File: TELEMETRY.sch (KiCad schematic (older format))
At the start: 0 parts

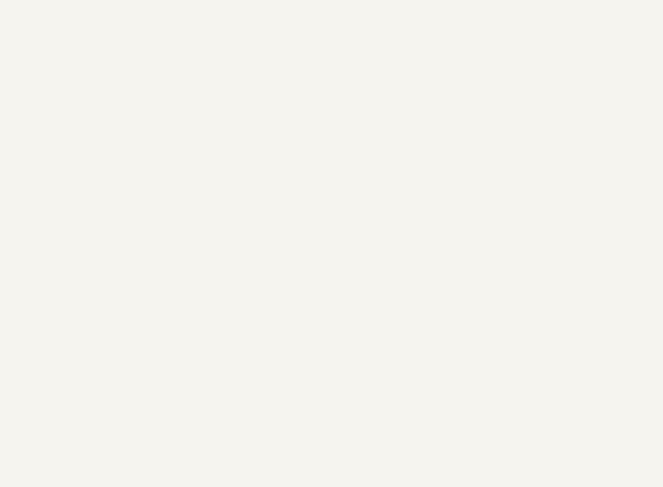
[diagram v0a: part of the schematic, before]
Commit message: Added RFM95
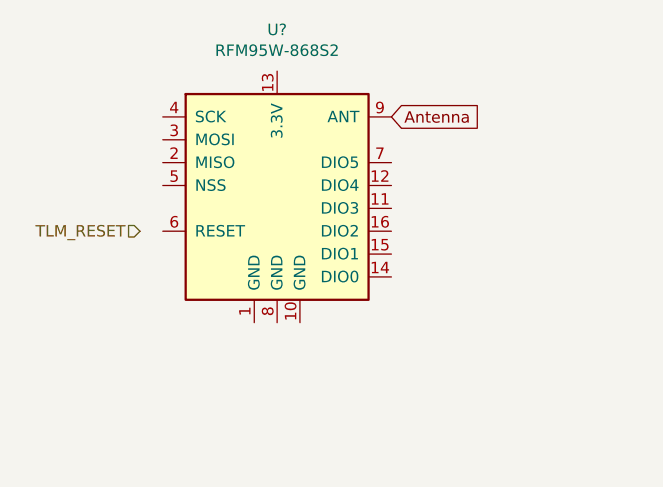
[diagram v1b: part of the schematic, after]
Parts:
- added U?: RFM95W-868S2, symbol RF_Module:RFM95W-868S2
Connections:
- new net Antenna: U?.9 (ANT)
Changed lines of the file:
@@
 $Descr A4 11693 8268
 encoding utf-8
-Sheet 4 9
+Sheet 9 9
 Title "TARS-MK1"
 Date ""
@@
 	1    0    0    -1
 $EndComp
+$Comp
+L RF_Module:RFM95W-868S2 U?
+U 1 1 5F8B4512
+P 3500 2950
+F 0 "U?" H 3500 3631 50  0000 C CNN
+F 1 "RFM95W-868S2" H 3500 3540 50  0000 C CNN
+F 2 "" H 200 4600 50  0001 C CNN
+F 3 "https://www.hoperf.com/data/upload/portal/20181127/5bfcbea20e9ef.pdf" H 200 4600 50  0001 C CNN
+	1    3500 2950
+	1    0    0    -1
+$EndComp
+Text GLabel 4000 2650 2    50   Input ~ 0
+Antenna
+Text HLabel 2900 3150 0    50   Input ~ 0
+TLM_RESET
 $EndSCHEMATC

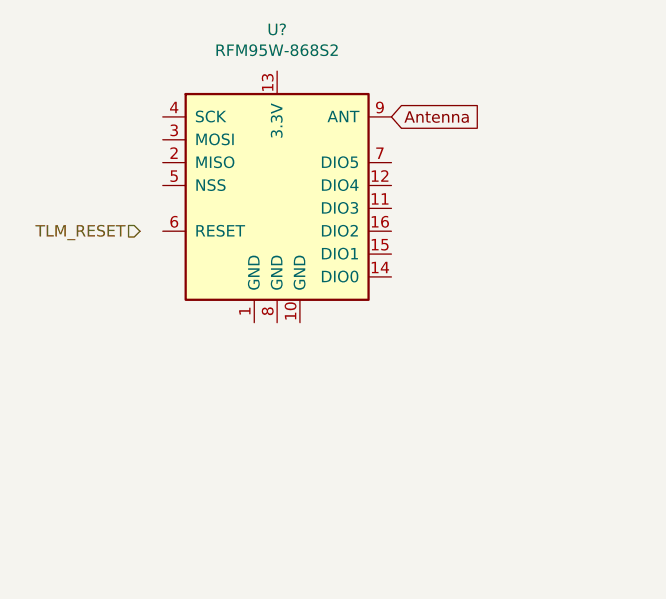
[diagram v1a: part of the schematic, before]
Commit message: Added labels to RFM95
Hierarchical and global labels added, as well as sheet labels
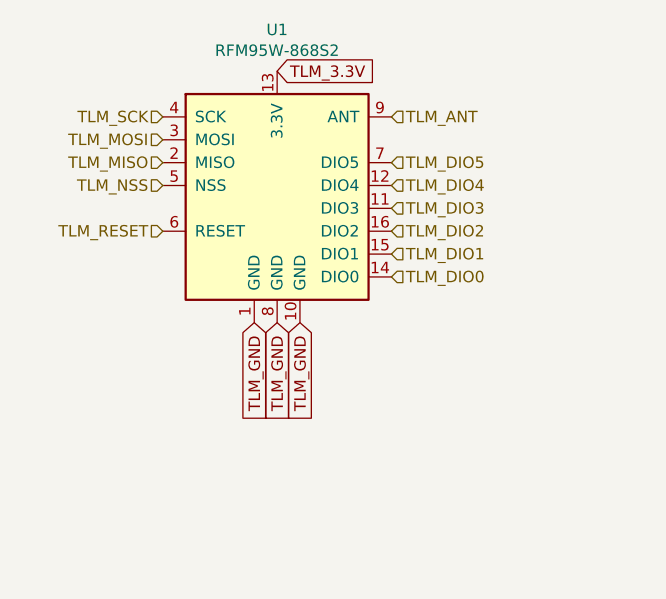
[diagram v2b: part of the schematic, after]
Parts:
- gave numbers to parts that had none: 1
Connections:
- net TLM_RESET: now also U1.6 (RESET)
- net TLM_GND: now reaches U1.1 (GND)
- net TLM_GND: now also U1.10 (GND), U1.8 (GND)
- net TLM_DIO3: now reaches U1.11 (DIO3)
- net TLM_DIO4: now reaches U1.12 (DIO4)
- net TLM_3.3V: now reaches U1.13 (3.3V)
- net TLM_DIO0: now reaches U1.14 (DIO0)
- net TLM_DIO1: now reaches U1.15 (DIO1)
- net TLM_DIO2: now reaches U1.16 (DIO2)
- net TLM_MISO: now reaches U1.2 (MISO)
- net TLM_MOSI: now reaches U1.3 (MOSI)
- net TLM_SCK: now reaches U1.4 (SCK)
- net TLM_NSS: now reaches U1.5 (NSS)
- net TLM_DIO5: now reaches U1.7 (DIO5)
- net Antenna renamed TLM_ANT
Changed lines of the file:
@@
 $EndDescr
 $Comp
-L ISS_LOGO:LOGO #G?
+L ISS_LOGO:LOGO #G9
 U 1 1 5F87BCA1
 P 7600 6800
-F 0 "#G?" H 7600 6677 60  0001 C CNN
+F 0 "#G9" H 7600 6677 60  0001 C CNN
 F 1 "LOGO" H 7600 6923 60  0001 C CNN
 F 2 "" H 7600 6800 50  0001 C CNN
@@
 	1    0    0    -1
 $EndComp
+Text HLabel 3000 3150 0    50   Input ~ 0
+TLM_RESET
+Text HLabel 4000 2650 2    50   Input ~ 0
+TLM_ANT
+Text HLabel 3000 2650 0    50   Input ~ 0
+TLM_SCK
+Text HLabel 3000 2750 0    50   Input ~ 0
+TLM_MOSI
+Text HLabel 3000 2850 0    50   Input ~ 0
+TLM_MISO
+Text HLabel 3000 2950 0    50   Input ~ 0
+TLM_NSS
+Text GLabel 3400 3550 3    50   Input ~ 0
+TLM_GND
+Text GLabel 3500 3550 3    50   Input ~ 0
+TLM_GND
+Text GLabel 3600 3550 3    50   Input ~ 0
+TLM_GND
+Text HLabel 4000 2850 2    50   Input ~ 0
+TLM_DIO5
+Text HLabel 4000 2950 2    50   Input ~ 0
+TLM_DIO4
+Text HLabel 4000 3050 2    50   Input ~ 0
+TLM_DIO3
+Text HLabel 4000 3150 2    50   Input ~ 0
+TLM_DIO2
+Text HLabel 4000 3250 2    50   Input ~ 0
+TLM_DIO1
+Text HLabel 4000 3350 2    50   Input ~ 0
+TLM_DIO0
 $Comp
-L RF_Module:RFM95W-868S2 U?
+L RF_Module:RFM95W-868S2 U1
 U 1 1 5F8B4512
 P 3500 2950
-F 0 "U?" H 3500 3631 50  0000 C CNN
+F 0 "U1" H 3500 3631 50  0000 C CNN
 F 1 "RFM95W-868S2" H 3500 3540 50  0000 C CNN
 F 2 "" H 200 4600 50  0001 C CNN
@@
 	1    0    0    -1
 $EndComp
-Text GLabel 4000 2650 2    50   Input ~ 0
-Antenna
-Text HLabel 2900 3150 0    50   Input ~ 0
-TLM_RESET
+Text GLabel 3500 2450 2    50   Input ~ 0
+TLM_3.3V
 $EndSCHEMATC

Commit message: Added SMA connector
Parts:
- added X1: SMACONNECTOR, symbol SMA_CONNECTOR:SMACONNECTOR
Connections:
- net labels added: 3.3V_IN, GND
- net labels removed: TLM_3.3V, TLM_ANT, TLM_GND
- wire segments 0 -> 10
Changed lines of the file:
@@
 Text HLabel 3000 3150 0    50   Input ~ 0
 TLM_RESET
-Text HLabel 4000 2650 2    50   Input ~ 0
-TLM_ANT
 Text HLabel 3000 2650 0    50   Input ~ 0
 TLM_SCK
@@
 Text HLabel 3000 2950 0    50   Input ~ 0
 TLM_NSS
-Text GLabel 3400 3550 3    50   Input ~ 0
-TLM_GND
-Text GLabel 3500 3550 3    50   Input ~ 0
-TLM_GND
-Text GLabel 3600 3550 3    50   Input ~ 0
-TLM_GND
 Text HLabel 4000 2850 2    50   Input ~ 0
 TLM_DIO5
@@
 $EndComp
 Text GLabel 3500 2450 2    50   Input ~ 0
-TLM_3.3V
+3.3V_IN
+$Comp
+L power:GND #PWR01
+U 1 1 5F947841
+P 3500 3700
+F 0 "#PWR01" H 3500 3450 50  0001 C CNN
+F 1 "GND" H 3505 3527 50  0000 C CNN
+F 2 "" H 3500 3700 50  0001 C CNN
+F 3 "" H 3500 3700 50  0001 C CNN
+	1    3500 3700
+	1    0    0    -1
+$EndComp
+Wire Wire Line
+	3400 3550 3500 3550
+Connection ~ 3500 3550
+Wire Wire Line
+	3500 3550 3600 3550
+Wire Wire Line
+	3500 3550 3500 3700
+$Comp
+L SMA_CONNECTOR:SMACONNECTOR X1
+U 1 1 5F9480D1
+P 4800 2650
+F 0 "X1" H 5030 2696 50  0000 L CNN
+F 1 "SMACONNECTOR" H 5030 2605 50  0000 L CNN
+F 2 "" H 4800 2650 50  0001 C CNN
+F 3 "" H 4800 2650 50  0001 C CNN
+	1    4800 2650
+	1    0    0    -1
+$EndComp
+Wire Wire Line
+	4000 2650 4500 2650
+$Comp
+L power:GND #PWR03
+U 1 1 5F949889
+P 4800 3050
+F 0 "#PWR03" H 4800 2800 50  0001 C CNN
+F 1 "GND" H 4805 2877 50  0000 C CNN
+F 2 "" H 4800 3050 50  0001 C CNN
+F 3 "" H 4800 3050 50  0001 C CNN
+	1    4800 3050
+	1    0    0    -1
+$EndComp
+Wire Wire Line
+	4700 2950 4800 2950
+Wire Wire Line
+	4800 2950 4800 3050
+Connection ~ 4800 2950
+Wire Wire Line
+	4800 2950 4900 2950
+$Comp
+L power:GND #PWR02
+U 1 1 5F949FA5
+P 4800 2250
+F 0 "#PWR02" H 4800 2000 50  0001 C CNN
+F 1 "GND" H 4805 2077 50  0000 C CNN
+F 2 "" H 4800 2250 50  0001 C CNN
+F 3 "" H 4800 2250 50  0001 C CNN
+	1    4800 2250
+	-1   0    0    1
+$EndComp
+Wire Wire Line
+	4700 2350 4800 2350
+Wire Wire Line
+	4800 2350 4800 2250
+Connection ~ 4800 2350
+Wire Wire Line
+	4800 2350 4900 2350
 $EndSCHEMATC

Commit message: Fixes library paths
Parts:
- removed X1: SMACONNECTOR, symbol SMA_CONNECTOR:SMACONNECTOR
- added X?: SMACONNECTOR, symbol SMA:SMACONNECTOR
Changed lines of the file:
@@
 $Descr A4 11693 8268
 encoding utf-8
-Sheet 9 9
+Sheet 10 10
 Title "TARS-MK1"
 Date ""
@@
 Wire Wire Line
 	3500 3550 3500 3700
-$Comp
-L SMA_CONNECTOR:SMACONNECTOR X1
-U 1 1 5F9480D1
-P 4800 2650
-F 0 "X1" H 5030 2696 50  0000 L CNN
-F 1 "SMACONNECTOR" H 5030 2605 50  0000 L CNN
-F 2 "" H 4800 2650 50  0001 C CNN
-F 3 "" H 4800 2650 50  0001 C CNN
-	1    4800 2650
-	1    0    0    -1
-$EndComp
 Wire Wire Line
 	4000 2650 4500 2650
@@
 Wire Wire Line
 	4800 2350 4900 2350
+$Comp
+L SMA:SMACONNECTOR X?
+U 1 1 5F94DDFD
+P 4800 2650
+F 0 "X?" H 5030 2696 50  0000 L CNN
+F 1 "SMACONNECTOR" H 5030 2605 50  0000 L CNN
+F 2 "" H 4800 2650 50  0001 C CNN
+F 3 "" H 4800 2650 50  0001 C CNN
+	1    4800 2650
+	1    0    0    -1
+$EndComp
 $EndSCHEMATC

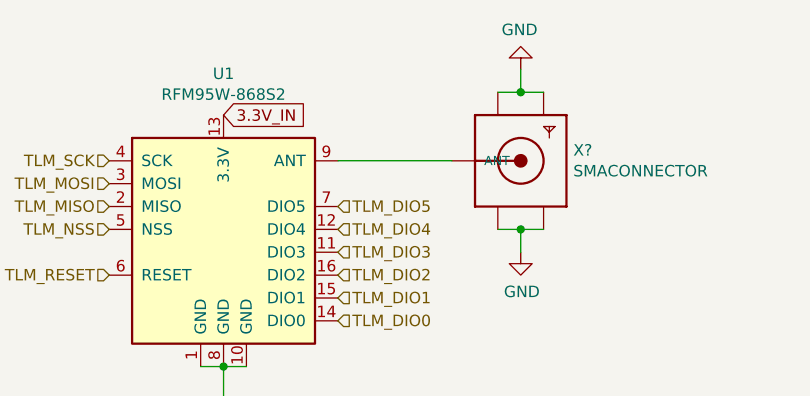
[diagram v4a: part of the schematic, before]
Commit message: Made library for D25V50F5 5V step-down
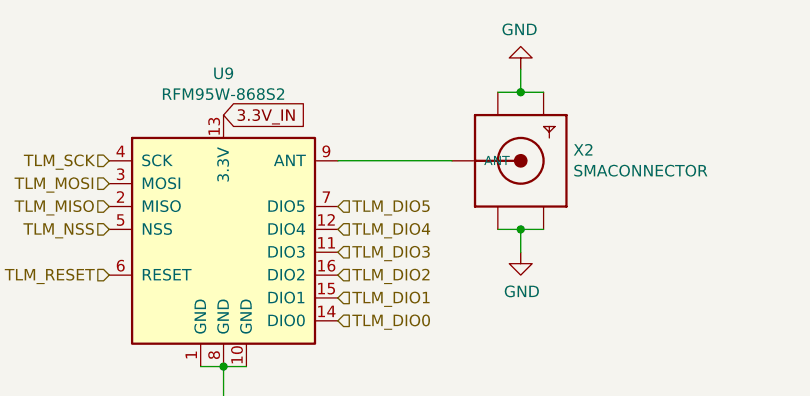
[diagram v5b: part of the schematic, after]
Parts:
- gave numbers to parts that had none: 1
- renumbered U1 to U9
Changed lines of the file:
@@
 TLM_DIO0
 $Comp
-L RF_Module:RFM95W-868S2 U1
+L RF_Module:RFM95W-868S2 U9
 U 1 1 5F8B4512
 P 3500 2950
-F 0 "U1" H 3500 3631 50  0000 C CNN
+F 0 "U9" H 3500 3631 50  0000 C CNN
 F 1 "RFM95W-868S2" H 3500 3540 50  0000 C CNN
 F 2 "" H 200 4600 50  0001 C CNN
@@
 3.3V_IN
 $Comp
-L power:GND #PWR01
+L power:GND #PWR020
 U 1 1 5F947841
 P 3500 3700
-F 0 "#PWR01" H 3500 3450 50  0001 C CNN
+F 0 "#PWR020" H 3500 3450 50  0001 C CNN
 F 1 "GND" H 3505 3527 50  0000 C CNN
 F 2 "" H 3500 3700 50  0001 C CNN
@@
 	4000 2650 4500 2650
 $Comp
-L power:GND #PWR03
+L power:GND #PWR022
 U 1 1 5F949889
 P 4800 3050
-F 0 "#PWR03" H 4800 2800 50  0001 C CNN
+F 0 "#PWR022" H 4800 2800 50  0001 C CNN
 F 1 "GND" H 4805 2877 50  0000 C CNN
 F 2 "" H 4800 3050 50  0001 C CNN
@@
 	4800 2950 4900 2950
 $Comp
-L power:GND #PWR02
+L power:GND #PWR021
 U 1 1 5F949FA5
 P 4800 2250
-F 0 "#PWR02" H 4800 2000 50  0001 C CNN
+F 0 "#PWR021" H 4800 2000 50  0001 C CNN
 F 1 "GND" H 4805 2077 50  0000 C CNN
 F 2 "" H 4800 2250 50  0001 C CNN
@@
 	4800 2350 4900 2350
 $Comp
-L SMA:SMACONNECTOR X?
+L SMA:SMACONNECTOR X2
 U 1 1 5F94DDFD
 P 4800 2650
-F 0 "X?" H 5030 2696 50  0000 L CNN
+F 0 "X2" H 5030 2696 50  0000 L CNN
 F 1 "SMACONNECTOR" H 5030 2605 50  0000 L CNN
 F 2 "" H 4800 2650 50  0001 C CNN

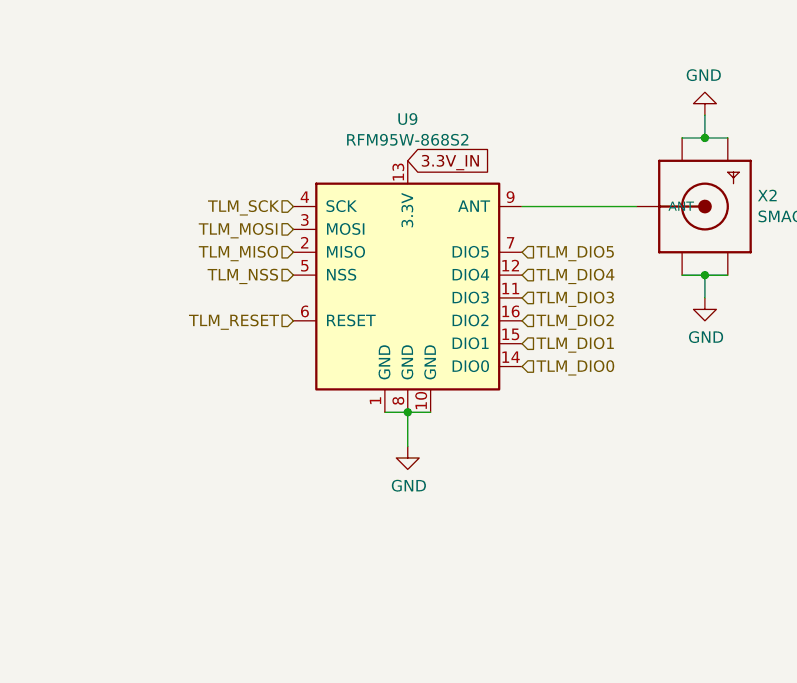
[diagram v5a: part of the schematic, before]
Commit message: Connected MPU, reorganized power system, cleaned libraries, created BBB footprint
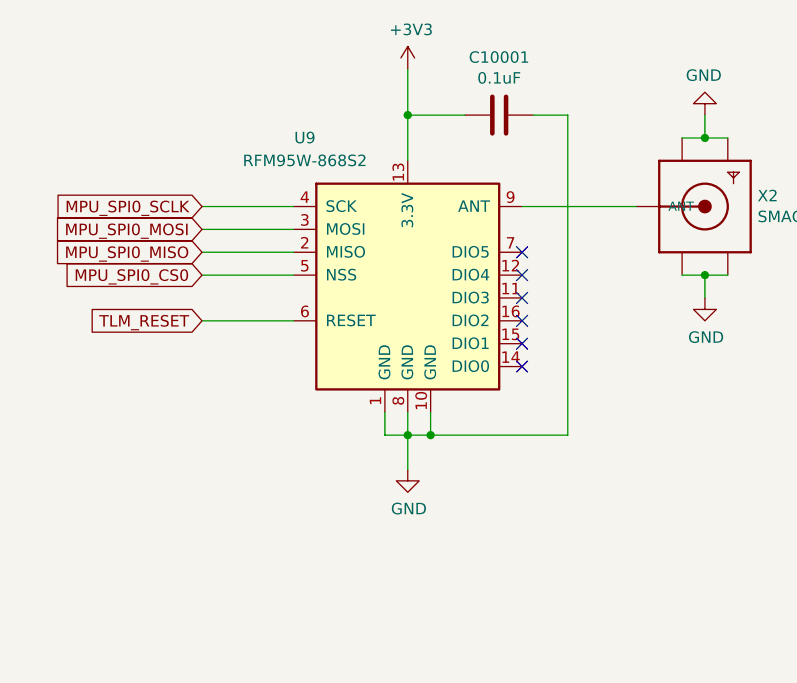
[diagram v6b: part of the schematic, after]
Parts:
- added C10001: 0.1uF, symbol D24V50F5:C
- X2: footprint (none) -> SMA:SMA90_DIP
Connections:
- net GND: now also C10001.1
- net 3.3V_IN renamed +3V3
- net +3V3: now also C10001.2
- net TLM_DIO0: no longer names the net of U9.14 (DIO0)
- net TLM_DIO1: no longer names the net of U9.15 (DIO1)
- net TLM_DIO2: no longer names the net of U9.16 (DIO2)
- net TLM_DIO3: no longer names the net of U9.11 (DIO3)
- net TLM_DIO4: no longer names the net of U9.12 (DIO4)
- net TLM_DIO5: no longer names the net of U9.7 (DIO5)
- net TLM_MISO renamed MPU_SPI0_MISO
- net TLM_MOSI renamed MPU_SPI0_MOSI
- net TLM_NSS renamed MPU_SPI0_CS0
- net TLM_SCK renamed MPU_SPI0_SCLK
- no-connect marks 0 -> 6
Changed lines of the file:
@@
 	1    0    0    -1
 $EndComp
-Text HLabel 3000 3150 0    50   Input ~ 0
-TLM_RESET
-Text HLabel 3000 2650 0    50   Input ~ 0
-TLM_SCK
-Text HLabel 3000 2750 0    50   Input ~ 0
-TLM_MOSI
-Text HLabel 3000 2850 0    50   Input ~ 0
-TLM_MISO
-Text HLabel 3000 2950 0    50   Input ~ 0
-TLM_NSS
-Text HLabel 4000 2850 2    50   Input ~ 0
-TLM_DIO5
-Text HLabel 4000 2950 2    50   Input ~ 0
-TLM_DIO4
-Text HLabel 4000 3050 2    50   Input ~ 0
-TLM_DIO3
-Text HLabel 4000 3150 2    50   Input ~ 0
-TLM_DIO2
-Text HLabel 4000 3250 2    50   Input ~ 0
-TLM_DIO1
-Text HLabel 4000 3350 2    50   Input ~ 0
-TLM_DIO0
-$Comp
-L RF_Module:RFM95W-868S2 U9
-U 1 1 5F8B4512
-P 3500 2950
-F 0 "U9" H 3500 3631 50  0000 C CNN
-F 1 "RFM95W-868S2" H 3500 3540 50  0000 C CNN
-F 2 "" H 200 4600 50  0001 C CNN
-F 3 "https://www.hoperf.com/data/upload/portal/20181127/5bfcbea20e9ef.pdf" H 200 4600 50  0001 C CNN
-	1    3500 2950
-	1    0    0    -1
-$EndComp
-Text GLabel 3500 2450 2    50   Input ~ 0
-3.3V_IN
 $Comp
 L power:GND #PWR020
 U 1 1 5F947841
-P 3500 3700
-F 0 "#PWR020" H 3500 3450 50  0001 C CNN
-F 1 "GND" H 3505 3527 50  0000 C CNN
-F 2 "" H 3500 3700 50  0001 C CNN
-F 3 "" H 3500 3700 50  0001 C CNN
-	1    3500 3700
+P 3500 3800
+F 0 "#PWR020" H 3500 3550 50  0001 C CNN
+F 1 "GND" H 3505 3627 50  0000 C CNN
+F 2 "" H 3500 3800 50  0001 C CNN
+F 3 "" H 3500 3800 50  0001 C CNN
+	1    3500 3800
 	1    0    0    -1
 $EndComp
-Wire Wire Line
-	3400 3550 3500 3550
-Connection ~ 3500 3550
-Wire Wire Line
-	3500 3550 3600 3550
-Wire Wire Line
-	3500 3550 3500 3700
 Wire Wire Line
 	4000 2650 4500 2650
@@
 F 0 "X2" H 5030 2696 50  0000 L CNN
 F 1 "SMACONNECTOR" H 5030 2605 50  0000 L CNN
-F 2 "" H 4800 2650 50  0001 C CNN
+F 2 "SMA:SMA90_DIP" H 4800 2650 50  0001 C CNN
 F 3 "" H 4800 2650 50  0001 C CNN
 	1    4800 2650
 	1    0    0    -1
 $EndComp
+$Comp
+L power:+3V3 #PWR0134
+U 1 1 5F98F509
+P 3500 2050
+F 0 "#PWR0134" H 3500 1900 50  0001 C CNN
+F 1 "+3V3" H 3515 2223 50  0000 C CNN
+F 2 "" H 3500 2050 50  0001 C CNN
+F 3 "" H 3500 2050 50  0001 C CNN
+	1    3500 2050
+	1    0    0    -1
+$EndComp
+Wire Wire Line
+	3500 2050 3500 2250
+$Comp
+L D24V50F5:C C10001
+U 1 1 5F991F8E
+P 3900 2250
+F 0 "C10001" V 3648 2250 50  0000 C CNN
+F 1 "0.1uF" V 3739 2250 50  0000 C CNN
+F 2 "" H 3938 2100 50  0001 C CNN
+F 3 "~" H 3900 2250 50  0001 C CNN
+	1    3900 2250
+	0    1    1    0
+$EndComp
+Wire Wire Line
+	3750 2250 3500 2250
+Connection ~ 3500 2250
+Wire Wire Line
+	3500 2250 3500 2450
+Wire Wire Line
+	4050 2250 4200 2250
+Wire Wire Line
+	4200 2250 4200 3650
+Wire Wire Line
+	4200 3650 3600 3650
+$Comp
+L RF_Module:RFM95W-868S2 U9
+U 1 1 5F8B4512
+P 3500 2950
+F 0 "U9" H 3050 3550 50  0000 C CNN
+F 1 "RFM95W-868S2" H 3050 3450 50  0000 C CNN
+F 2 "" H 200 4600 50  0001 C CNN
+F 3 "https://www.hoperf.com/data/upload/portal/20181127/5bfcbea20e9ef.pdf" H 200 4600 50  0001 C CNN
+	1    3500 2950
+	1    0    0    -1
+$EndComp
+Wire Wire Line
+	3400 3550 3400 3650
+Wire Wire Line
+	3400 3650 3500 3650
+Connection ~ 3500 3650
+Wire Wire Line
+	3500 3550 3500 3650
+Wire Wire Line
+	3600 3550 3600 3650
+Connection ~ 3600 3650
+Wire Wire Line
+	3600 3650 3500 3650
+Wire Wire Line
+	3500 3650 3500 3800
+NoConn ~ 4000 2850
+NoConn ~ 4000 2950
+NoConn ~ 4000 3050
+NoConn ~ 4000 3150
+NoConn ~ 4000 3250
+NoConn ~ 4000 3350
+Text GLabel 2600 2850 0    50   Input ~ 0
+MPU_SPI0_MISO
+Wire Wire Line
+	3000 2850 2600 2850
+Text GLabel 2600 2650 0    50   Input ~ 0
+MPU_SPI0_SCLK
+Wire Wire Line
+	2600 2650 3000 2650
+Text GLabel 2600 2950 0    50   Input ~ 0
+MPU_SPI0_CS0
+Wire Wire Line
+	3000 2950 2600 2950
+Text GLabel 2600 2750 0    50   Input ~ 0
+MPU_SPI0_MOSI
+Wire Wire Line
+	2600 2750 3000 2750
+Text GLabel 2600 3150 0    50   Input ~ 0
+TLM_RESET
+Wire Wire Line
+	2600 3150 3000 3150
 $EndSCHEMATC
